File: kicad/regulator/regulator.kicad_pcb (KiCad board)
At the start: 2 copper layers, 40.6 x 20.3 mm, 10 parts, among them J1 Conn_01x02, J2 Conn_01x02

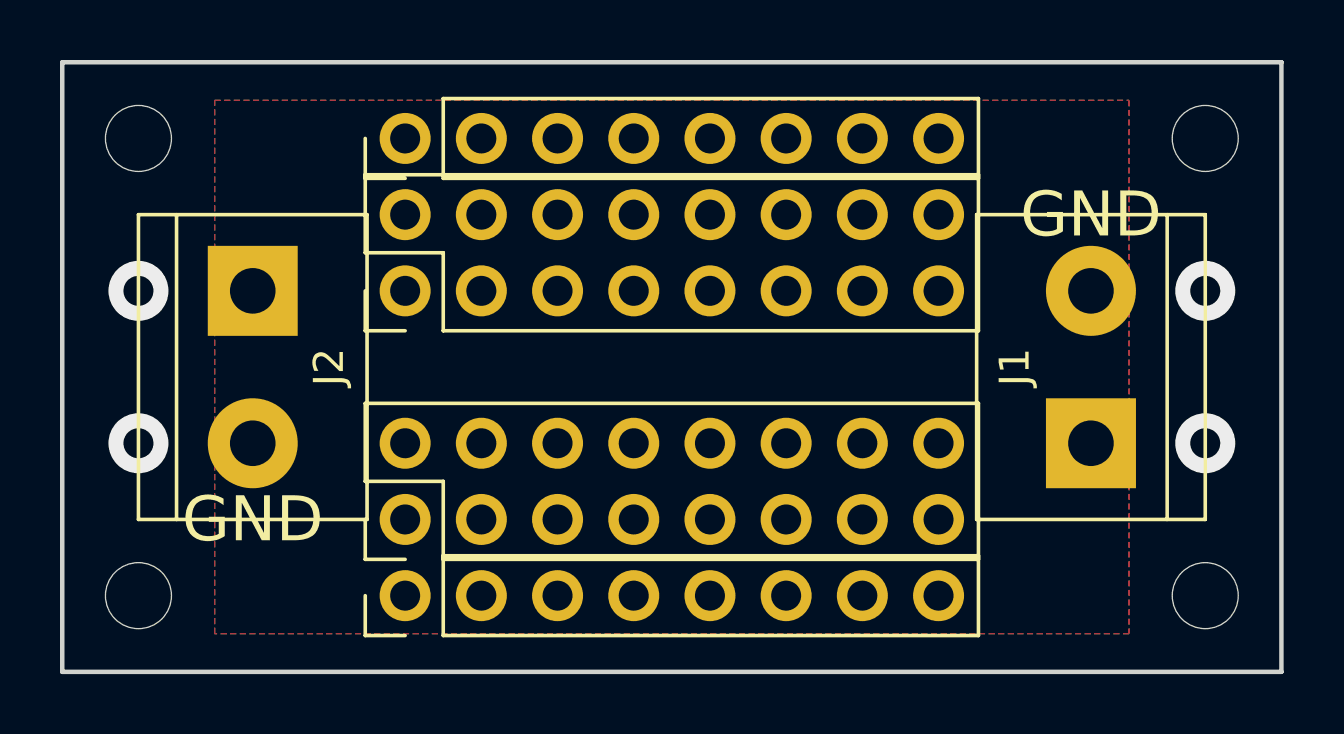
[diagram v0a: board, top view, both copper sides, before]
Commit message: add gnd holes
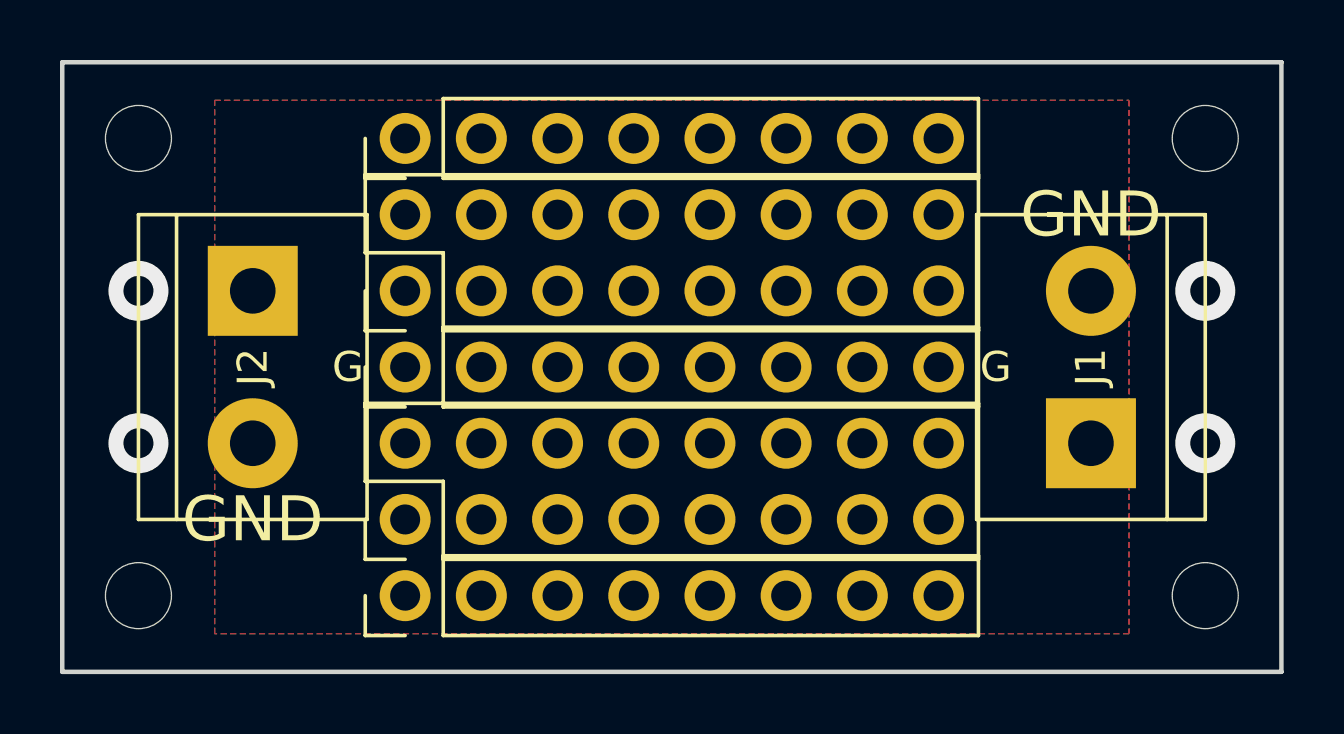
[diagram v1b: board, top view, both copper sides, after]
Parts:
- added J3: Conn_01x02, Connector_PinHeader_2.54mm:PinHeader_1x08_P2.54mm_Vertical, F.Cu at (158.8, 104.1)
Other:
- board text added: "G"
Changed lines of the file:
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@@
   (general
     (thickness 1.6)
-    (drawings 8)
+    (drawings 10)
     (tracks 4)
     (zones 0)
-    (modules 10)
+    (modules 11)
     (nets 4)
   )
@@
     (descr "simple 2-pin terminal block, pitch 5.08mm, revamped version of bornier2")
     (tags "terminal block bornier2")
-    (fp_text reference J1 (at 2.54 -2.54 90) (layer F.SilkS)
+    (fp_text reference J1 (at 2.54 0 90) (layer F.SilkS)
       (effects (font (size 1 1) (thickness 0.15)))
     )
@@
     (descr "simple 2-pin terminal block, pitch 5.08mm, revamped version of bornier2")
     (tags "terminal block bornier2")
-    (fp_text reference J2 (at 2.54 -2.54 270) (layer F.SilkS)
+    (fp_text reference J2 (at 2.54 0 270) (layer F.SilkS)
       (effects (font (size 1 1) (thickness 0.15)))
     )
@@
     )
   )
+  (module Connector_PinHeader_2.54mm:PinHeader_1x08_P2.54mm_Vertical (layer F.Cu)
+    (at 158.75 104.14 90)
+    (descr "Through hole straight pin header, 1x08, 2.54mm pitch, single row")
+    (tags "Through hole pin header THT 1x08 2.54mm single row")
+    (zone_connect 2)
+    (fp_text reference J3 (at 0 -2.33 90) (layer F.SilkS) hide
+      (effects (font (size 1 1) (thickness 0.15)))
+    )
+    (fp_text value Conn_01x02 (at 0 20.11 90) (layer F.Fab)
+      (effects (font (size 1 1) (thickness 0.15)))
+    )
+    (fp_line (start -0.635 -1.27) (end 1.27 -1.27) (layer F.Fab) (width 0.1))
+    (fp_line (start 1.27 -1.27) (end 1.27 19.05) (layer F.Fab) (width 0.1))
+    (fp_line (start 1.27 19.05) (end -1.27 19.05) (layer F.Fab) (width 0.1))
+    (fp_line (start -1.27 19.05) (end -1.27 -0.635) (layer F.Fab) (width 0.1))
+    (fp_line (start -1.27 -0.635) (end -0.635 -1.27) (layer F.Fab) (width 0.1))
+    (fp_line (start -1.33 19.11) (end 1.33 19.11) (layer F.SilkS) (width 0.12))
+    (fp_line (start -1.33 1.27) (end -1.33 19.11) (layer F.SilkS) (width 0.12))
+    (fp_line (start 1.33 1.27) (end 1.33 19.11) (layer F.SilkS) (width 0.12))
+    (fp_line (start -1.33 1.27) (end 1.33 1.27) (layer F.SilkS) (width 0.12))
+    (fp_line (start -1.33 0) (end -1.33 -1.33) (layer F.SilkS) (width 0.12))
+    (fp_line (start -1.33 -1.33) (end 0 -1.33) (layer F.SilkS) (width 0.12))
+    (fp_line (start -1.8 -1.8) (end -1.8 19.55) (layer F.CrtYd) (width 0.05))
+    (fp_line (start -1.8 19.55) (end 1.8 19.55) (layer F.CrtYd) (width 0.05))
+    (fp_line (start 1.8 19.55) (end 1.8 -1.8) (layer F.CrtYd) (width 0.05))
+    (fp_line (start 1.8 -1.8) (end -1.8 -1.8) (layer F.CrtYd) (width 0.05))
+    (fp_text user %R (at 0 8.89 180) (layer F.Fab)
+      (effects (font (size 1 1) (thickness 0.15)))
+    )
+    (pad 1 thru_hole circle (at 0 0 90) (size 1.7 1.7) (drill 1) (layers *.Cu *.Mask)
+      (net 2 GND) (zone_connect 2))
+    (pad 2 thru_hole oval (at 0 2.54 90) (size 1.7 1.7) (drill 1) (layers *.Cu *.Mask)
+      (net 2 GND) (zone_connect 2))
+    (pad 3 thru_hole oval (at 0 5.08 90) (size 1.7 1.7) (drill 1) (layers *.Cu *.Mask)
+      (net 2 GND) (zone_connect 2))
+    (pad 4 thru_hole oval (at 0 7.62 90) (size 1.7 1.7) (drill 1) (layers *.Cu *.Mask)
+      (net 2 GND) (zone_connect 2))
+    (pad 5 thru_hole oval (at 0 10.16 90) (size 1.7 1.7) (drill 1) (layers *.Cu *.Mask)
+      (net 2 GND) (zone_connect 2))
+    (pad 6 thru_hole oval (at 0 12.7 90) (size 1.7 1.7) (drill 1) (layers *.Cu *.Mask)
+      (net 2 GND) (zone_connect 2))
+    (pad 7 thru_hole oval (at 0 15.24 90) (size 1.7 1.7) (drill 1) (layers *.Cu *.Mask)
+      (net 2 GND) (zone_connect 2))
+    (pad 8 thru_hole oval (at 0 17.78 90) (size 1.7 1.7) (drill 1) (layers *.Cu *.Mask)
+      (net 2 GND) (zone_connect 2))
+    (model ${KISYS3DMOD}/Connector_PinHeader_2.54mm.3dshapes/PinHeader_1x08_P2.54mm_Vertical.wrl
+      (at (xyz 0 0 0))
+      (scale (xyz 1 1 1))
+      (rotate (xyz 0 0 0))
+    )
+  )
+  (gr_text G (at 156.845 104.14) (layer F.SilkS)
+    (effects (font (size 1 1) (thickness 0.12)))
+  )
+  (gr_text G (at 178.435 104.14) (layer F.SilkS)
+    (effects (font (size 1 1) (thickness 0.12)))
+  )
   (gr_text GND (at 153.67 109.22) (layer F.SilkS)
     (effects (font (size 1.5 1.5) (thickness 0.3)))
@@
     (effects (font (size 1.5 1.5) (thickness 0.3)))
   )
-  (dimension 20.32 (width 0.3) (layer Dwgs.User)
-    (gr_text "20.320 mm" (at 207.84 104.14 270) (layer Dwgs.User)
+  (dimension 20.32 (width 0.3) (layer Cmts.User)
+    (gr_text "20.320 mm" (at 207.84 104.14 270) (layer Cmts.User)
       (effects (font (size 1.5 1.5) (thickness 0.3)))
     )
@@
     (arrow2b (pts (xy 205.74 93.98) (xy 206.326421 95.106504)))
   )
-  (dimension 40.64 (width 0.3) (layer Dwgs.User)
-    (gr_text "40.640 mm" (at 167.64 124.02) (layer Dwgs.User)
+  (dimension 40.64 (width 0.3) (layer Cmts.User)
+    (gr_text "40.640 mm" (at 167.64 124.02) (layer Cmts.User)
       (effects (font (size 1.5 1.5) (thickness 0.3)))
     )
